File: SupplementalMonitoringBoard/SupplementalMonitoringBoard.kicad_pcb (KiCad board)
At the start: 2 copper layers, 129 x 134 mm, 44 parts, among them J1 PeripheralCANConnector, U1 OPA842xDBV, U2 OPA842xDBV, U3 INA180B1, U4 PAMC131M03QDFMRQ1, U5 PeripheralSOM

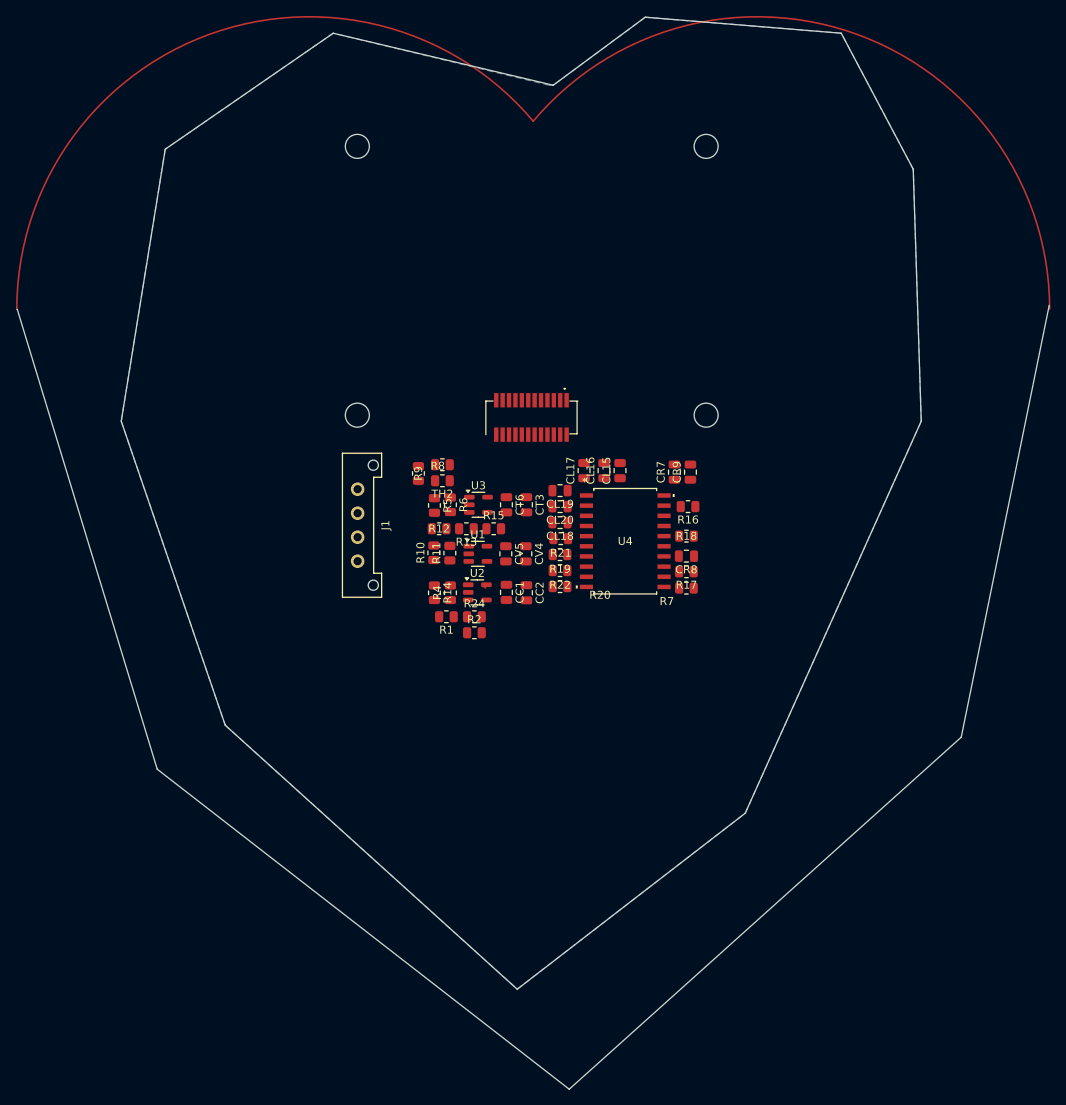
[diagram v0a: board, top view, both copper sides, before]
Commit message: PCB Layout - Supplemental Monitoring Board
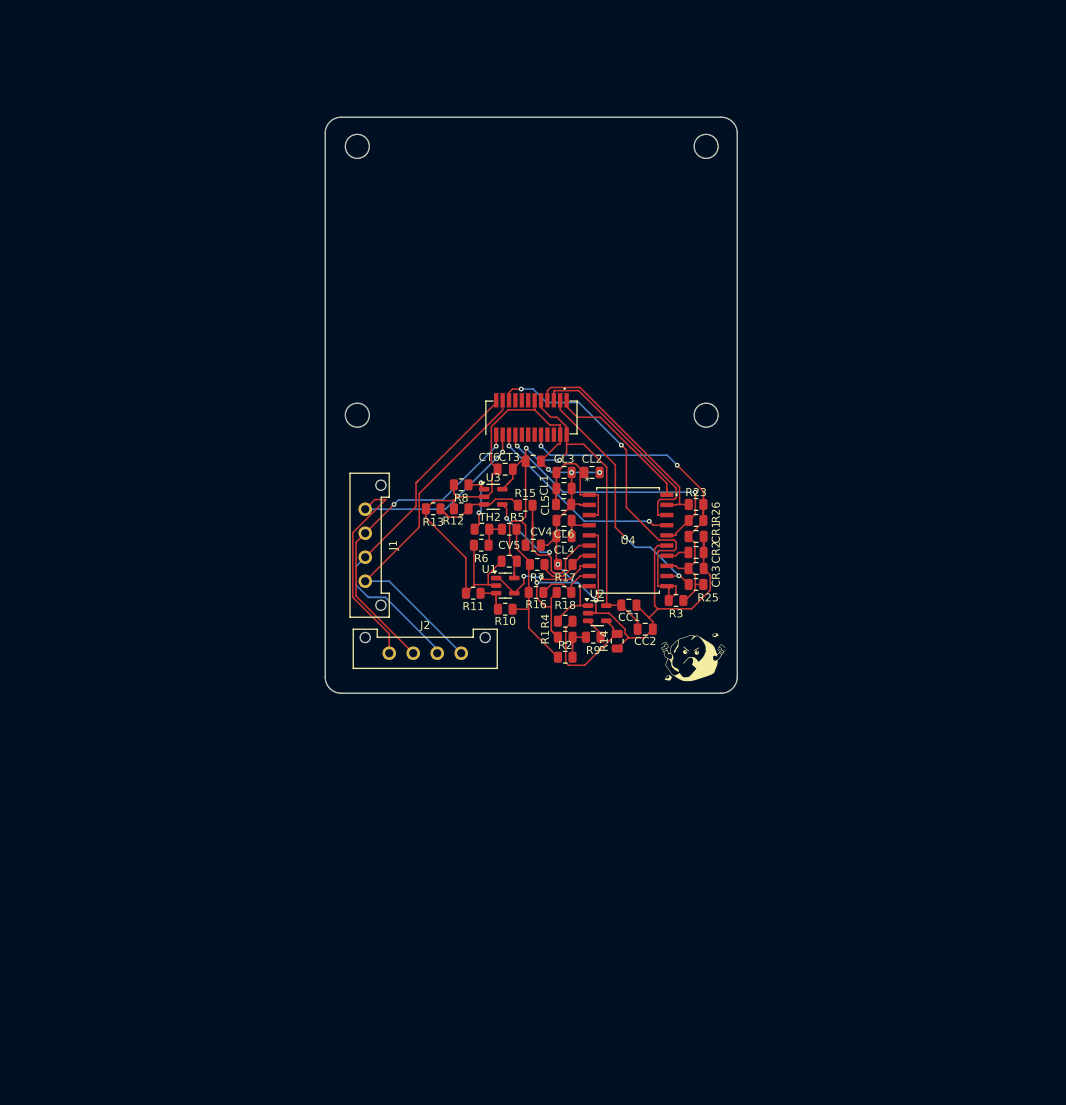
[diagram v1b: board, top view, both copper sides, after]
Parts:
- removed CL15, CL18, CR8: 100nF, Capacitor_SMD:C_0805_2012Metric
- removed CL16, CL19, CL20, CR7: 1nF, Capacitor_SMD:C_0805_2012Metric
- removed CL17, CR9: 1uF, Capacitor_SMD:C_0805_2012Metric
- removed R19, R20: 2.6k, Resistor_SMD:R_0805_2012Metric
- removed R21, R22: 10k, Resistor_SMD:R_0805_2012Metric
- removed R24: .33, Resistor_SMD:R_0805_2012Metric
- added CL1: 100nF, Capacitor_SMD:C_0805_2012Metric, F.Cu at (135.4, 104.9)
- added CL2: 1nF, Capacitor_SMD:C_0805_2012Metric, F.Cu at (138.9, 102.9)
- added CL3: 1uF, Capacitor_SMD:C_0805_2012Metric, F.Cu at (135.4, 102.9)
- added CL4: 100nF, Capacitor_SMD:C_0805_2012Metric, F.Cu at (135.4, 110.9)
- added CL5: 1nF, Capacitor_SMD:C_0805_2012Metric, F.Cu at (135.3, 106.9)
- added CL6: 1nF, Capacitor_SMD:C_0805_2012Metric, F.Cu at (135.4, 108.9)
- added CR1: 1nF, Capacitor_SMD:C_0805_2012Metric, F.Cu at (151.9, 110.9)
- added CR2: 100nF, Capacitor_SMD:C_0805_2012Metric, F.Cu at (151.9, 112.9)
- added CR3: 1uF, Capacitor_SMD:C_0805_2012Metric, F.Cu at (151.9, 114.9)
- added G***: LOGO, LOGO, F.Cu at (151.5, 126.0)
- added J2: PeripheralCANConnector, UTSVT_Connectors:Molex_MicroFit3.0_1x4xP3.00mm_PolarizingPeg_Vertical, F.Cu at (113.5, 125.5)
- added R23: 100k, Resistor_SMD:R_0805_2012Metric, F.Cu at (151.9, 106.9)
- added R25: 100k, Resistor_SMD:R_0805_2012Metric, F.Cu at (151.9, 116.9)
- added R26: 100k, Resistor_SMD:R_0805_2012Metric, F.Cu at (151.9, 108.9)
- added R3: 100k, Resistor_SMD:R_0805_2012Metric, F.Cu at (149.4, 118.9)
- R10, R5: value 30k -> 40k
- R14: value 10 -> 150K
- R15: value 5k -> 3k
- R16: value 100k -> 30k
- R17, R18: value 100k -> 10k
- R2: value 30k -> 50K
- R4: value 10k -> 10K
- R7: value 100k -> 30K
- R8, TH2: value 1k -> 500
- R9: value 1k -> .01
- moved R9 29.9 mm to (139.0, 123.5), turned to 180 degrees
- moved R14 23.6 mm to (142.0, 124.0), turned to 90 degrees
- moved R16 21.8 mm to (131.9, 117.9)
- moved R7 18.9 mm to (132.0, 114.4)
- moved R18 16.8 mm to (135.4, 117.9)
- moved CC2 15.5 mm to (145.5, 122.5), turned to 0 degrees
- moved CC1 15.4 mm to (143.4, 119.5), turned to 0 degrees
- moved U2 15.2 mm to (139.5, 120.5)
- moved R17 15.2 mm to (135.5, 114.4)
- moved R1 15.1 mm to (135.5, 123.5)
- moved R4 14.8 mm to (135.5, 121.5), turned to 180 degrees
- moved R2 11.8 mm to (135.5, 126.0), turned to 180 degrees
- moved R10 11.4 mm to (128.0, 120.0), turned to 0 degrees
- moved R5 9.81 mm to (128.5, 110.0), turned to 0 degrees
- moved TH2 7.81 mm to (125.1, 110.0)
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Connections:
- net /ADC Connect/DCDC_OUT renamed /DCDC_OUT
- R1 pad 1: Net-(U2-+) -> Net-(R1-Pad1)
- R16 pad 1: /LowPower -> /AINOP
- R16 pad 2: /*CS -> +BATT
- R17 pad 1: /LowPower -> /AIN12N
- R17 pad 2: /DOUT -> GND
- R18 pad 1: /LowPower -> /AINOP
- R18 pad 2: /*DRDY -> GND
- R2 pad 1: Net-(U2-+) -> Net-(R1-Pad1)
- R7 pad 1: /LowPower -> /AIN12N
- R7 pad 2: /*SYNC/*RESET -> +BATT
- R9 pad 1: /Temperature/Thermistor -> Net-(U2-+)
- R9 pad 2: Net-(U3-+) -> Net-(R1-Pad1)
- U3 pad 1: Net-(U3-+) -> /Temperature/Thermistor
- U4 pad 13: /ADC Output/DVDD -> /DVDD
- U4 pad 14: GND -> /DCDC_CAP
- U4 pad 15: /LowPower -> GND
- U4 pad 4: /ADC Connect/HLDO_OUT -> /HLDO_OUT
- U4 pad 7: /GNDVoltage/AIN12N -> /AIN12N
- U4 pad 9: /GNDVoltage/AIN0P -> /AINOP
- U5 pad 10: /LowPower -> /DVDD
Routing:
- net GND: track 0.00 -> 166.8 mm, vias 0 -> 6
- net +3.3V: track 0.44 -> 71.0 mm, vias 0 -> 2
- net +12V: track 0.00 -> 48.2 mm, vias 0 -> 1
- net /*SYNC/*RESET: track 0.00 -> 47.5 mm, vias 0 -> 2
- net /DVDD: track 0.00 -> 45.7 mm, vias 0 -> 2
- net /CAN_L: track 0.00 -> 45.5 mm
- net /CAN_H: track 0.00 -> 44.6 mm
- net GNDPWR: track 0.00 -> 40.8 mm, vias 0 -> 2
- net /*DRDY: track 0.00 -> 33.7 mm, vias 0 -> 2
- net /DOUT: track 0.00 -> 32.4 mm, vias 0 -> 2
- net /AIN2P/GPO: track 0.00 -> 29.7 mm, vias 0 -> 2
- net /SCLK: track 0.00 -> 28.0 mm
- net /*CS: track 0.00 -> 28.0 mm
- net /CLKIN: track 0.00 -> 25.2 mm, vias 0 -> 2
- net +BATT: track 0.00 -> 20.8 mm
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- removed copper zone on B.Cu, net GND
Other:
- board size 129 x 134 mm -> 51.5 x 72 mm

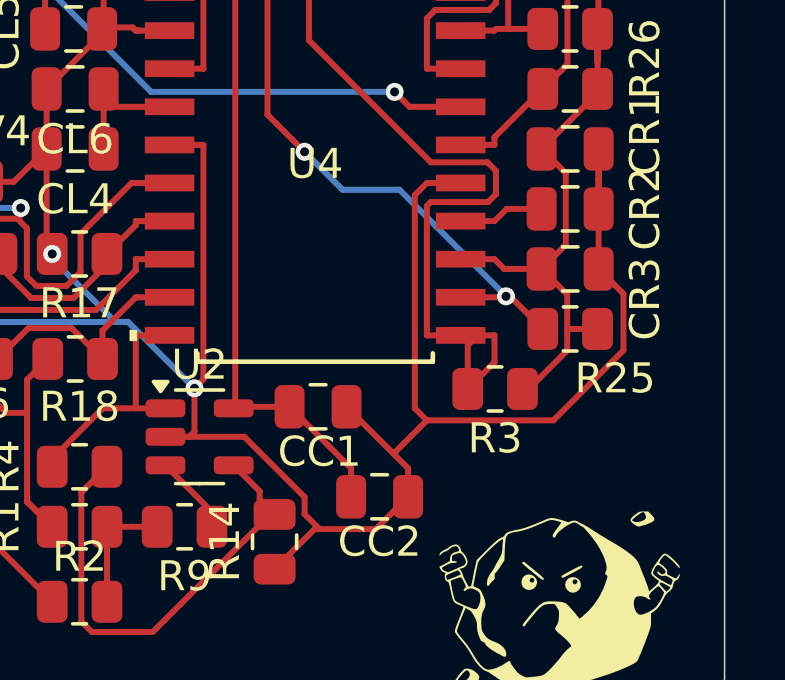
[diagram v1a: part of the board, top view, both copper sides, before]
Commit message: Supplemental Monitoring Board - Layout
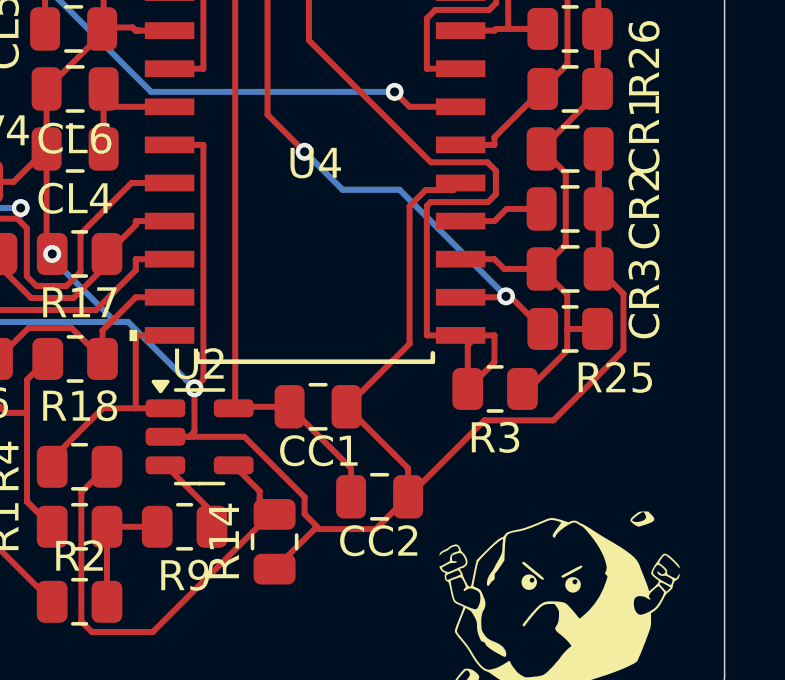
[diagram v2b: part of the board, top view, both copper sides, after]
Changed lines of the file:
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@@
-	)
-	(segment
-		(start 151.294 119.952)
-		(end 147.076 119.952)
-		(width 0.2)
-		(layer "F.Cu")
-		(net 1)
 	)
 	(segment
@@
 	)
 	(segment
+		(start 151.294 119.952)
+		(end 148.998 119.952)
+		(width 0.2)
+		(layer "F.Cu")
+		(net 1)
+	)
+	(segment
 		(start 144.4 119.5)
 		(end 145.964 121.064)
@@
 	)
 	(segment
+		(start 148.998 119.952)
+		(end 146.45 122.5)
+		(width 0.2)
+		(layer "F.Cu")
+		(net 1)
+	)
+	(segment
 		(start 134.439 117.905)
 		(end 133.748 118.596)
@@
 	)
 	(segment
-		(start 147.076 112.04)
-		(end 146.674 112.442)
-		(width 0.2)
-		(layer "F.Cu")
-		(net 1)
-	)
-	(segment
 		(start 143.335 123.577)
 		(end 143.5 123.577)
@@
 	)
 	(segment
+		(start 147.037315 112.275)
+		(end 146.5 112.812315)
+		(width 0.2)
+		(layer "F.Cu")
+		(net 1)
+	)
+	(segment
 		(start 138.5 106.96)
 		(end 137.474 106.96)
@@
 	)
 	(segment
+		(start 146.5 112.812315)
+		(end 146.5 117.4)
+		(width 0.2)
+		(layer "F.Cu")
+		(net 1)
+	)
+	(segment
 		(start 134.494 114.312)
 		(end 134.401 114.219)
@@
 	)
 	(segment
+		(start 146.5 117.4)
+		(end 144.4 119.5)
+		(width 0.2)
+		(layer "F.Cu")
+		(net 1)
+	)
+	(segment
 		(start 152.801 111.905)
 		(end 152.801 112.905)
@@
 	)
 	(segment
-		(start 148.2028 112.04)
-		(end 147.076 112.04)
-		(width 0.2)
-		(layer "F.Cu")
-		(net 1)
-	)
-	(segment
 		(start 152.801 110.905)
 		(end 152.801 111.905)
@@
 	)
 	(segment
-		(start 146.674 119.55)
-		(end 147.076 119.952)
-		(width 0.2)
-		(layer "F.Cu")
-		(net 1)
-	)
-	(segment
 		(start 134.588 123.5)
 		(end 133.748 122.66)
@@
 	)
 	(segment
-		(start 146.674 112.442)
-		(end 146.674 119.55)
-		(width 0.2)
-		(layer "F.Cu")
-		(net 1)
-	)
-	(segment
 		(start 136.3014 102.905)
 		(end 136.301 102.905)
@@
 	)
 	(segment
-		(start 147.076 119.952)
-		(end 145.964 121.064)
+		(start 147.9678 112.275)
+		(end 147.037315 112.275)
 		(width 0.2)
 		(layer "F.Cu")
@@
 		(width 0.2)
 		(layer "F.Cu")
+		(net 1)
+	)
+	(segment
+		(start 148.2028 112.04)
+		(end 147.9678 112.275)
+		(width 0.2)
+		(layer "F.Cu")

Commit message: Supplemental_Monitoring_Board
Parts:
- added ?: , , F.Cu at (124.5, 129.0)
- added ?: , , F.Cu at (167.5, 129.0)
- moved R13 49.1 mm to (167.3, 116.2), turned to 0 degrees
- moved R8 42.6 mm to (162.2, 119.8), turned to 0 degrees
- moved R12 42.2 mm to (163.8, 116.2), turned to 180 degrees
- moved R6 42.0 mm to (165.8, 121.8), turned to 0 degrees
- moved R11 40.9 mm to (163.9, 109.2), turned to 0 degrees
- moved TH2 39.0 mm to (162.3, 121.8)
- moved R5 38.6 mm to (165.8, 119.8)
- moved R10 38.2 mm to (164.0, 107.3)
- moved R2 36.2 mm to (161.4, 100.8), turned to 0 degrees
- moved R1 35.8 mm to (161.3, 98.8), turned to 0 degrees
- moved U3 34.9 mm to (159.7, 116.7), turned to 180 degrees
- moved R7 33.4 mm to (164.1, 105.2), turned to 0 degrees
- moved U1 32.7 mm to (159.9, 110.2), turned to 180 degrees
- moved R16 32.2 mm to (163.8, 113.9), turned to 0 degrees
- moved R4 31.9 mm to (161.4, 102.9)
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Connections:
- J1 pad 1: +12V -> +BATT
- J2 pad 1: +12V -> +BATT
- U5 pad 22: +12V -> +BATT
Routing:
- net +BATT: track 20.8 -> 102.8 mm, vias 0 -> 4
- net +12V: track 48.2 -> 0.00 mm, vias 1 -> 0
- net GND: track 167.1 -> 131.7 mm, vias 6 -> 5
- net /*SYNC/*RESET: track 47.5 -> 12.9 mm, vias 2 -> 4
- net +3.3V: track 71.0 -> 38.4 mm
- net /CAN_L: track 45.5 -> 65.5 mm, vias 0 -> 5
- net /DVDD: track 45.7 -> 29.6 mm, vias 2 -> 0
- net /DIN: track 19.4 -> 34.4 mm, vias 0 -> 2
- net /AINOP: track 7.99 -> 22.8 mm, vias 0 -> 2
- net /AIN2P/GPO: track 29.7 -> 14.9 mm, vias 2 -> 0
- net /*CS: track 28.0 -> 40.7 mm
- net /*DRDY: track 33.7 -> 23.2 mm
- net /AIN12N: track 8.24 -> 17.5 mm, vias 0 -> 2
- net /CLKIN: track 25.2 -> 17.3 mm
- net /DOUT: track 32.4 -> 25.9 mm, vias 2 -> 4
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- added copper zone on F.Cu, net GND
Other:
- board size 51.5 x 72 mm -> 53.5 x 77 mm

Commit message: Supplemental MOnitoring Board
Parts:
- removed the ? at (124.5, 129.0)
- removed the ? at (167.5, 129.0)
- removed G***: LOGO, LOGO
- added ?: , , F.Cu at (167.9, 129.8)
- added ?: , , F.Cu at (124.3, 129.8)
- added J3: CANconn2, Connector_Molex:Molex_Micro-Fit_3.0_43650-0215_1x02_P3.00mm_Vertical, F.Cu at (123.5, 110.8)
- CC1, CT3, CV5: value .1uF -> 1nF
- CL2, CL5, CL6, CR1: value 1nF -> .1uF
- J1: value PeripheralCANConnector -> CarPowerConnector; footprint UTSVT_Connectors:Molex_MicroFit3.0_1x4xP3.00mm_PolarizingPeg_Vertical -> Connector_Molex:Molex_Micro-Fit_3.0_43650-0215_1x02_P3.00mm_Vertical
- J2: value PeripheralCANConnector -> CANconn; footprint UTSVT_Connectors:Molex_MicroFit3.0_1x4xP3.00mm_PolarizingPeg_Vertical -> Connector_Molex:Molex_Micro-Fit_3.0_43650-0215_1x02_P3.00mm_Vertical
- R14: value 150K -> 150k
- R2: value 50K -> 50k
- R4: value 10K -> 10k
- R7: value 30K -> 30k
- TH2: value 500 -> 500.
- moved J1 23.9 mm to (143.0, 126.6), turned to 180 degrees
- moved R16 18.1 mm to (152.0, 100.2)
- moved R7 11.2 mm to (153.0, 107.2)
- moved J2 10.9 mm to (123.5, 122.2), turned to 90 degrees
- moved R18 10.3 mm to (148.7, 100.2), turned to 180 degrees
- moved R14 9.28 mm to (162.6, 102.9), turned to 180 degrees
- moved R5 8.92 mm to (157.5, 116.5), turned to 180 degrees
- moved R17 7.32 mm to (153.0, 109.2)
- moved R6 6.95 mm to (159.6, 118.5), turned to 180 degrees
- moved R2 5.89 mm to (155.5, 100.2), turned to 180 degrees
- moved CT3 5.44 mm to (157.5, 114.5)
- moved CT6 5.43 mm to (157.5, 112.5)
- moved R8 4.33 mm to (165.2, 116.5)
- moved CV4 4.22 mm to (157.5, 109.9)
- moved CV5 4.08 mm to (157.5, 107.9)
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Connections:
- J1 pad 1: +BATT -> +12V
- J1 pad 2: GNDPWR -> GND
- J2 pad 1: +BATT -> /CAN_L
- J2 pad 2: GNDPWR -> /CAN_H
- R10 pad 2: +BATT -> +12V
- R16 pad 2: +BATT -> +12V
- R2 pad 2: +BATT -> +12V
- R5 pad 2: +BATT -> +12V
- R7 pad 2: +BATT -> +12V
- U5 pad 10: /DVDD -> unconnected-(U5-VDDA(3.3V)-Pad10)
- U5 pad 22: +BATT -> +12V
- U5 pad 9: +3.3V -> /DVDD
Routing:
- net +BATT: track 102.8 -> 0.00 mm, vias 4 -> 0
- net GND: track 131.7 -> 38.1 mm, vias 5 -> 9
- net +12V: track 0.00 -> 87.0 mm, vias 0 -> 6
- net GNDPWR: track 42.8 -> 0.00 mm, vias 4 -> 0
- net /AINOP: track 22.8 -> 5.97 mm
- net /AIN12N: track 17.5 -> 7.46 mm
- net +3.3V: track 38.4 -> 29.3 mm, vias 2 -> 6
- net /CAN_H: track 48.8 -> 42.9 mm, vias 4 -> 2
- net /AIN0N: track 11.4 -> 16.9 mm
- net /CAN_L: track 65.5 -> 70.9 mm
- net /DVDD: track 29.6 -> 33.8 mm, vias 0 -> 2
- net /SCLK: track 30.8 -> 27.3 mm
- net Net-(U3--): track 8.75 -> 5.66 mm
- net /AIN2P/GPO: track 14.9 -> 17.4 mm, vias 0 -> 4
- net Net-(R1-Pad1): track 3.87 -> 6.04 mm
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- added copper zone on B.Cu, net GND

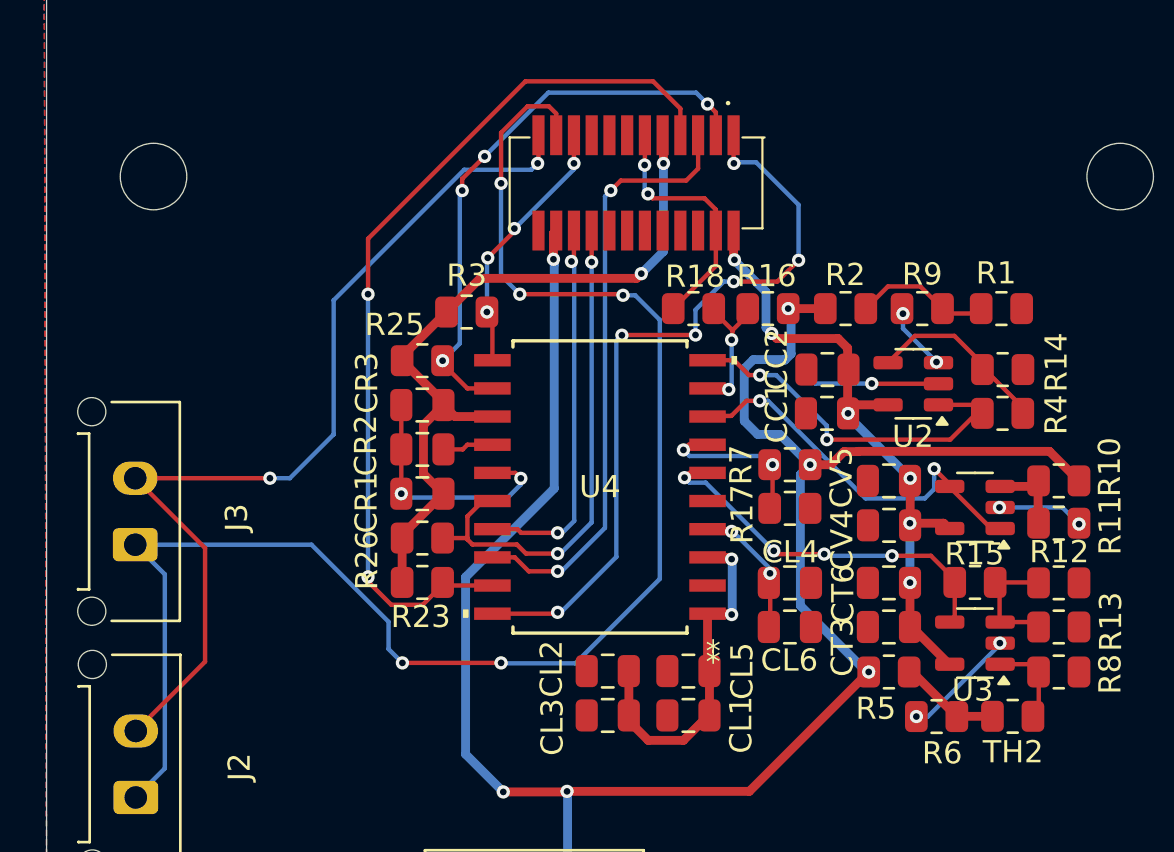
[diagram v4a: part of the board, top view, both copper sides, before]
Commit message: Supplemental Monitoring Board
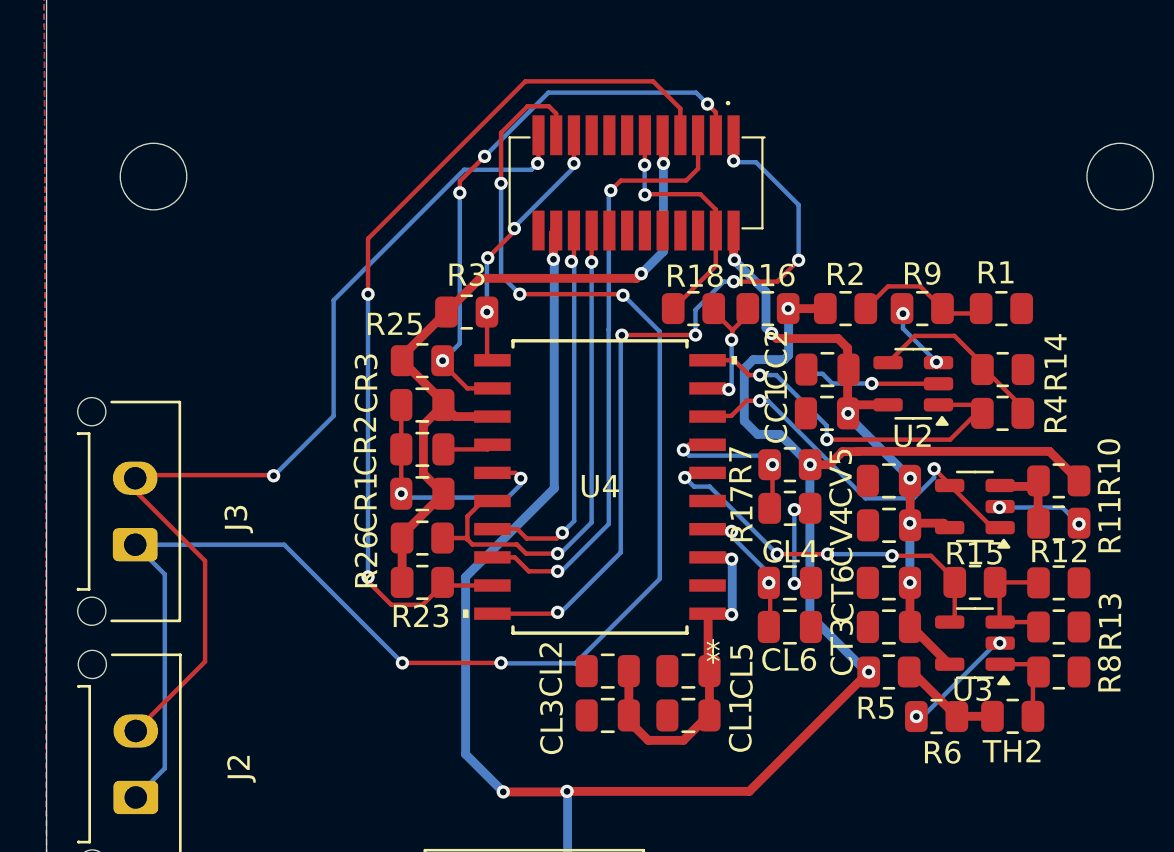
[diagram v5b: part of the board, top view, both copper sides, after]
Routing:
- net GND: track 38.1 -> 43.0 mm, vias 9 -> 11
- net /CAN_L: track 70.9 -> 69.8 mm
